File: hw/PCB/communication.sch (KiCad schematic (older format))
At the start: 2 parts, among them J3 SMA, U4 RFM69HCW

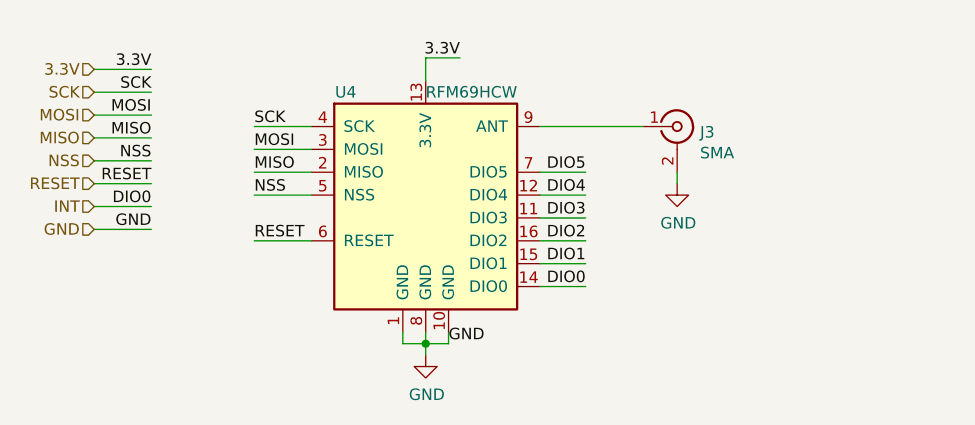
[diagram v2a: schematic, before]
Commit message: Added new connections and 3D models. Most components are now placed in the PCB.
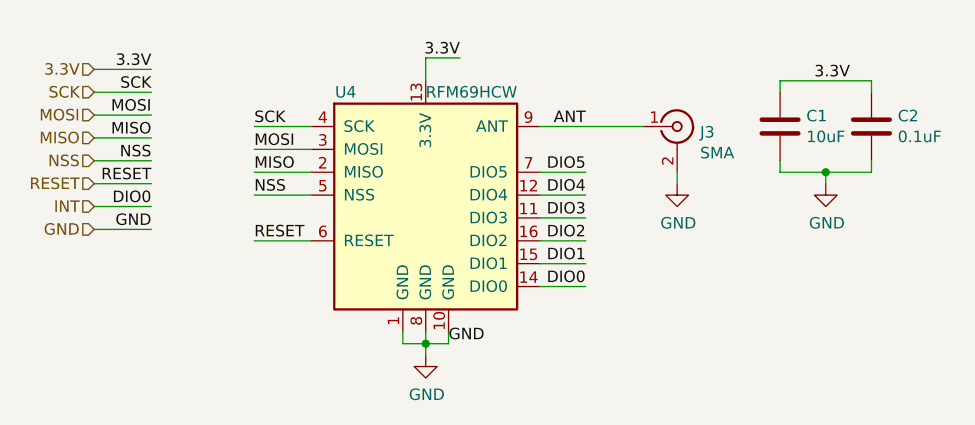
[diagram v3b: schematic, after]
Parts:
- added C1: 10uF, Capacitor_SMD:C_0603_1608Metric_Pad1.05x0.95mm_HandSolder, symbol Device:C
- added C2: 0.1uF, Capacitor_SMD:C_0603_1608Metric_Pad1.05x0.95mm_HandSolder, symbol Device:C
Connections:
- net 3.3V: now also C1.1, C2.1
- net GND: now also C1.2, C2.2
- net ANT: now reaches J3.1 (In), U4.9 (ANT)
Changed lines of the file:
@@
 Wire Wire Line
 	6700 3450 6700 3500
+Text Label 6300 3250 2    50   ~ 0
+ANT
+$Comp
+L Device:C C2
+U 1 1 5BF35059
+P 7550 3250
+F 0 "C2" H 7435 3296 50  0000 R CNN
+F 1 "0.1uF" H 7435 3205 50  0000 R CNN
+F 2 "Capacitor_SMD:C_0603_1608Metric_Pad1.05x0.95mm_HandSolder" H 7588 3100 50  0001 C CNN
+F 3 "~" H 7550 3250 50  0001 C CNN
+	1    7550 3250
+	-1   0    0    -1
+$EndComp
+$Comp
+L Device:C C1
+U 1 1 5BF354AB
+P 7150 3250
+F 0 "C1" H 7265 3296 50  0000 L CNN
+F 1 "10uF" H 7265 3205 50  0000 L CNN
+F 2 "Capacitor_SMD:C_0603_1608Metric_Pad1.05x0.95mm_HandSolder" H 7188 3100 50  0001 C CNN
+F 3 "~" H 7150 3250 50  0001 C CNN
+	1    7150 3250
+	1    0    0    -1
+$EndComp
+Wire Wire Line
+	7150 3400 7150 3450
+Wire Wire Line
+	7150 3450 7350 3450
+Wire Wire Line
+	7550 3450 7550 3400
+Wire Wire Line
+	7350 3450 7350 3500
+Connection ~ 7350 3450
+Wire Wire Line
+	7350 3450 7550 3450
+Wire Wire Line
+	7150 3100 7150 3050
+Wire Wire Line
+	7150 3050 7550 3050
+Wire Wire Line
+	7550 3050 7550 3100
+Text Label 7300 3050 0    50   ~ 0
+3.3V
+$Comp
+L power:GND #PWR0113
+U 1 1 5BF39227
+P 7350 3500
+F 0 "#PWR0113" H 7350 3250 50  0001 C CNN
+F 1 "GND" H 7355 3327 50  0000 C CNN
+F 2 "" H 7350 3500 50  0001 C CNN
+F 3 "" H 7350 3500 50  0001 C CNN
+	1    7350 3500
+	1    0    0    -1
+$EndComp
 $EndSCHEMATC

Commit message: Updated the RFM69HCW symbol and created a new SAMD21E symbol.
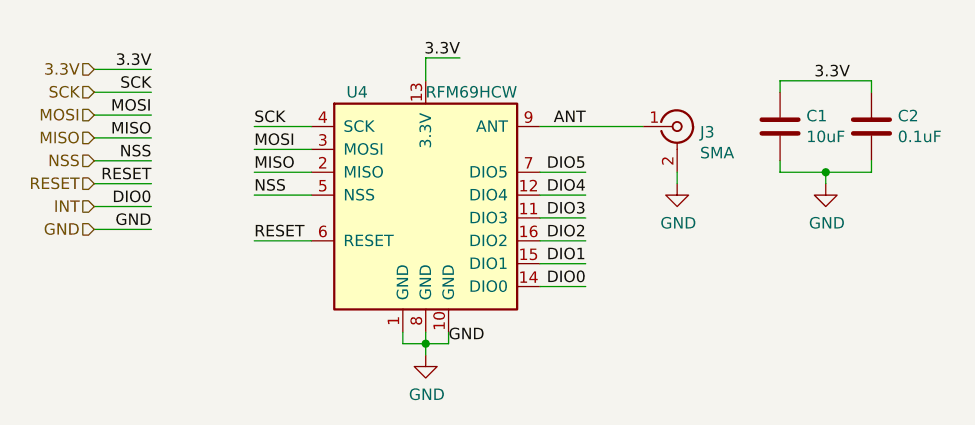
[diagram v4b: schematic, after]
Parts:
- removed U4: RFM69HCW, Transceptor:RFM69HCW, symbol RF_AM_FM:RFM69HCW
- added U4: RFM69HCW, symbol RF_Module:RFM69HCW
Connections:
- net 3.3V: now also U4.13 (3.3V)
- net ANT: now also U4.9 (ANT)
- net DIO1: now also U4.15 (DIO1)
- net DIO2: now also U4.16 (DIO2)
- net DIO3: now also U4.11 (DIO3)
- net DIO4: now also U4.12 (DIO4)
- net DIO5: now also U4.7 (DIO5)
- net GND: now also U4.1 (GND), U4.10 (GND), U4.8 (GND)
- net INT: now also U4.14 (DIO0)
- net MISO: now also U4.2 (MISO)
- net MOSI: now also U4.3 (MOSI)
- net NSS: now also U4.5 (NSS)
- net RESET: now also U4.6 (RESET)
- net SCK: now also U4.4 (SCK)
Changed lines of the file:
@@
-EESchema Schematic File Version 4
+EESchema Schematic File Version 5
 LIBS:FOD-cache
 EELAYER 29 0
@@
 Comment4 ""
 $EndDescr
-$Comp
-L RF_AM_FM:RFM69HCW U4
-U 1 1 5BD13EFB
-P 5600 3550
-F 0 "U4" H 5250 4000 50  0000 C CNN
-F 1 "RFM69HCW" H 5800 4000 50  0000 C CNN
-F 2 "Transceptor:RFM69HCW" H 2300 5200 50  0001 C CNN
-F 3 "http://www.hoperf.com/upload/rf/RFM69HCW-V1.1.pdf" H 2300 5200 50  0001 C CNN
-	1    5600 3550
-	1    0    0    -1
-$EndComp
 $Comp
 L antenna:SMA J3
@@
 	1    0    0    -1
 $EndComp
+$Comp
+L RF_Module:RFM69HCW U4
+U 1 1 5CF85C91
+P 5600 3550
+F 0 "U4" H 5300 4000 50  0000 C CNN
+F 1 "RFM69HCW" H 5800 4000 50  0000 C CNN
+F 2 "" H 2300 5200 50  0001 C CNN
+F 3 "https://www.hoperf.com/data/upload/portal/20181127/5bfcb8284d838.pdf" H 2300 5200 50  0001 C CNN
+	1    5600 3550
+	1    0    0    -1
+$EndComp

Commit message: Finished preliminary design phase for the version 2.0.
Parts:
- U3: renamed from U4; footprint (none) -> Transceptor:RFM69HCW
- renumbered J3 to J2
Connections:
- net 3.3V renamed +3V3
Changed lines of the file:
@@
 EESchema Schematic File Version 5
-LIBS:FOD-cache
 EELAYER 29 0
 EELAYER END
 $Descr A4 11693 8268
 encoding utf-8
-Sheet 4 5
+Sheet 4 6
 Title ""
 Date ""
@@
 $EndDescr
 $Comp
-L antenna:SMA J3
+L antenna:SMA J2
 U 1 1 5BD153FD
 P 6700 3250
-F 0 "J3" H 6800 3225 50  0000 L CNN
+F 0 "J2" H 6800 3225 50  0000 L CNN
 F 1 "SMA" H 6800 3134 50  0000 L CNN
 F 2 "Antenna:SMA" H 6700 3250 50  0001 C CNN
@@
 Wire Wire Line
 	6300 3450 6100 3450
-Wire Wire Line
-	5600 3050 5600 2950
-Wire Wire Line
-	5600 2950 5750 2950
-Text Label 5750 2950 2    50   ~ 0
-3.3V
 Text HLabel 4150 3000 0    50   Input ~ 0
-3.3V
+3V3
 Text HLabel 4150 3100 0    50   Input ~ 0
 SCK
@@
 SCK
 Text Label 4400 3000 2    50   ~ 0
-3.3V
+3V3
 $Comp
 L power:GND #PWR0110
@@
 	7150 3100 7150 3050
 Wire Wire Line
-	7150 3050 7550 3050
+	7150 3050 7350 3050
 Wire Wire Line
 	7550 3050 7550 3100
-Text Label 7300 3050 0    50   ~ 0
-3.3V
+Text Label 7150 3050 0    50   ~ 0
+3V3
 $Comp
 L power:GND #PWR0113
@@
 $EndComp
 $Comp
-L RF_Module:RFM69HCW U4
+L RF_Module:RFM69HCW U3
 U 1 1 5CF85C91
 P 5600 3550
-F 0 "U4" H 5300 4000 50  0000 C CNN
+F 0 "U3" H 5300 4000 50  0000 C CNN
 F 1 "RFM69HCW" H 5800 4000 50  0000 C CNN
-F 2 "" H 2300 5200 50  0001 C CNN
+F 2 "Transceptor:RFM69HCW" H 2300 5200 50  0001 C CNN
 F 3 "https://www.hoperf.com/data/upload/portal/20181127/5bfcb8284d838.pdf" H 2300 5200 50  0001 C CNN
 	1    5600 3550
 	1    0    0    -1
 $EndComp
+$Comp
+L power:+3V3 #PWR0115
+U 1 1 5D239D97
+P 5600 3000
+F 0 "#PWR0115" H 5600 2850 50  0001 C CNN
+F 1 "+3V3" H 5615 3173 50  0000 C CNN
+F 2 "" H 5600 3000 50  0001 C CNN
+F 3 "" H 5600 3000 50  0001 C CNN
+	1    5600 3000
+	1    0    0    -1
+$EndComp
+Wire Wire Line
+	5600 3050 5600 3000
+$Comp
+L power:+3V3 #PWR0116
+U 1 1 5D23A856
+P 7350 3000
+F 0 "#PWR0116" H 7350 2850 50  0001 C CNN
+F 1 "+3V3" H 7365 3173 50  0000 C CNN
+F 2 "" H 7350 3000 50  0001 C CNN
+F 3 "" H 7350 3000 50  0001 C CNN
+	1    7350 3000
+	1    0    0    -1
+$EndComp
+Wire Wire Line
+	7350 3000 7350 3050
+Connection ~ 7350 3050
+Wire Wire Line
+	7350 3050 7550 3050
 $EndSCHEMATC

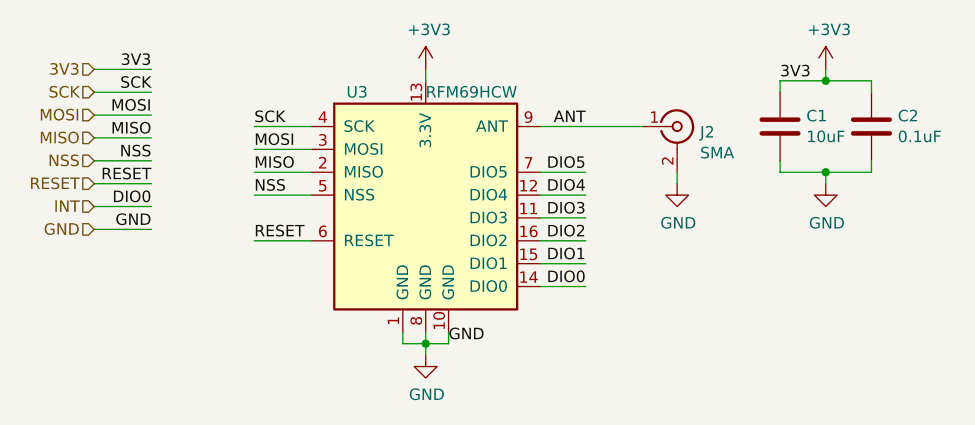
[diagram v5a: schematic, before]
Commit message: Replaced the SMA connector with an U.FL connector. Added some layout improvements.
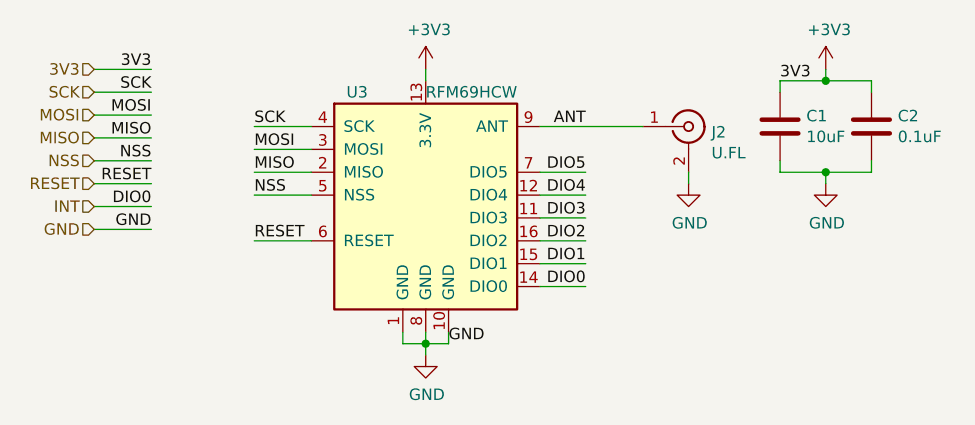
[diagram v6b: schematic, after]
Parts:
- removed J2: SMA, Antenna:SMA, symbol antenna:SMA
- added J2: U.FL, Connector_Coaxial:U.FL_Hirose_U.FL-R-SMT-1_Vertical, symbol Connector:Conn_Coaxial
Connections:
- net ANT: now also J2.1 (In)
- net GND: now also J2.2 (Ext)
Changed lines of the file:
@@
 EESchema Schematic File Version 5
+LIBS:FOD-cache
 EELAYER 29 0
 EELAYER END
@@
 Comment4 ""
 $EndDescr
-$Comp
-L antenna:SMA J2
-U 1 1 5BD153FD
-P 6700 3250
-F 0 "J2" H 6800 3225 50  0000 L CNN
-F 1 "SMA" H 6800 3134 50  0000 L CNN
-F 2 "Antenna:SMA" H 6700 3250 50  0001 C CNN
-F 3 "" H 6700 3250 50  0001 C CNN
-	1    6700 3250
-	1    0    0    -1
-$EndComp
 Wire Wire Line
 	5500 4150 5500 4200
@@
 Text Label 4400 3000 2    50   ~ 0
 3V3
-$Comp
-L power:GND #PWR0110
-U 1 1 5BD2EB6A
-P 6700 3500
-F 0 "#PWR0110" H 6700 3250 50  0001 C CNN
-F 1 "GND" H 6705 3327 50  0000 C CNN
-F 2 "" H 6700 3500 50  0001 C CNN
-F 3 "" H 6700 3500 50  0001 C CNN
-	1    6700 3500
-	1    0    0    -1
-$EndComp
-Wire Wire Line
-	6700 3450 6700 3500
+Wire Wire Line
+	6750 3450 6750 3500
 Text Label 6300 3250 2    50   ~ 0
 ANT
@@
 Wire Wire Line
 	7350 3050 7550 3050
+$Comp
+L Connector:Conn_Coaxial J2
+U 1 1 5D24F571
+P 6750 3250
+F 0 "J2" H 6850 3225 50  0000 L CNN
+F 1 "U.FL" H 6850 3134 50  0000 L CNN
+F 2 "Connector_Coaxial:U.FL_Hirose_U.FL-R-SMT-1_Vertical" H 6750 3250 50  0001 C CNN
+F 3 " ~" H 6750 3250 50  0001 C CNN
+	1    6750 3250
+	1    0    0    -1
+$EndComp
+$Comp
+L power:GND #PWR0110
+U 1 1 5BD2EB6A
+P 6750 3500
+F 0 "#PWR0110" H 6750 3250 50  0001 C CNN
+F 1 "GND" H 6755 3327 50  0000 C CNN
+F 2 "" H 6750 3500 50  0001 C CNN
+F 3 "" H 6750 3500 50  0001 C CNN
+	1    6750 3500
+	1    0    0    -1
+$EndComp
 $EndSCHEMATC
